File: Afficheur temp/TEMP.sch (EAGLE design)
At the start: 24 parts, among them IC1 MCP23008P, IC2 MCP23008P, X1 22-23-2041

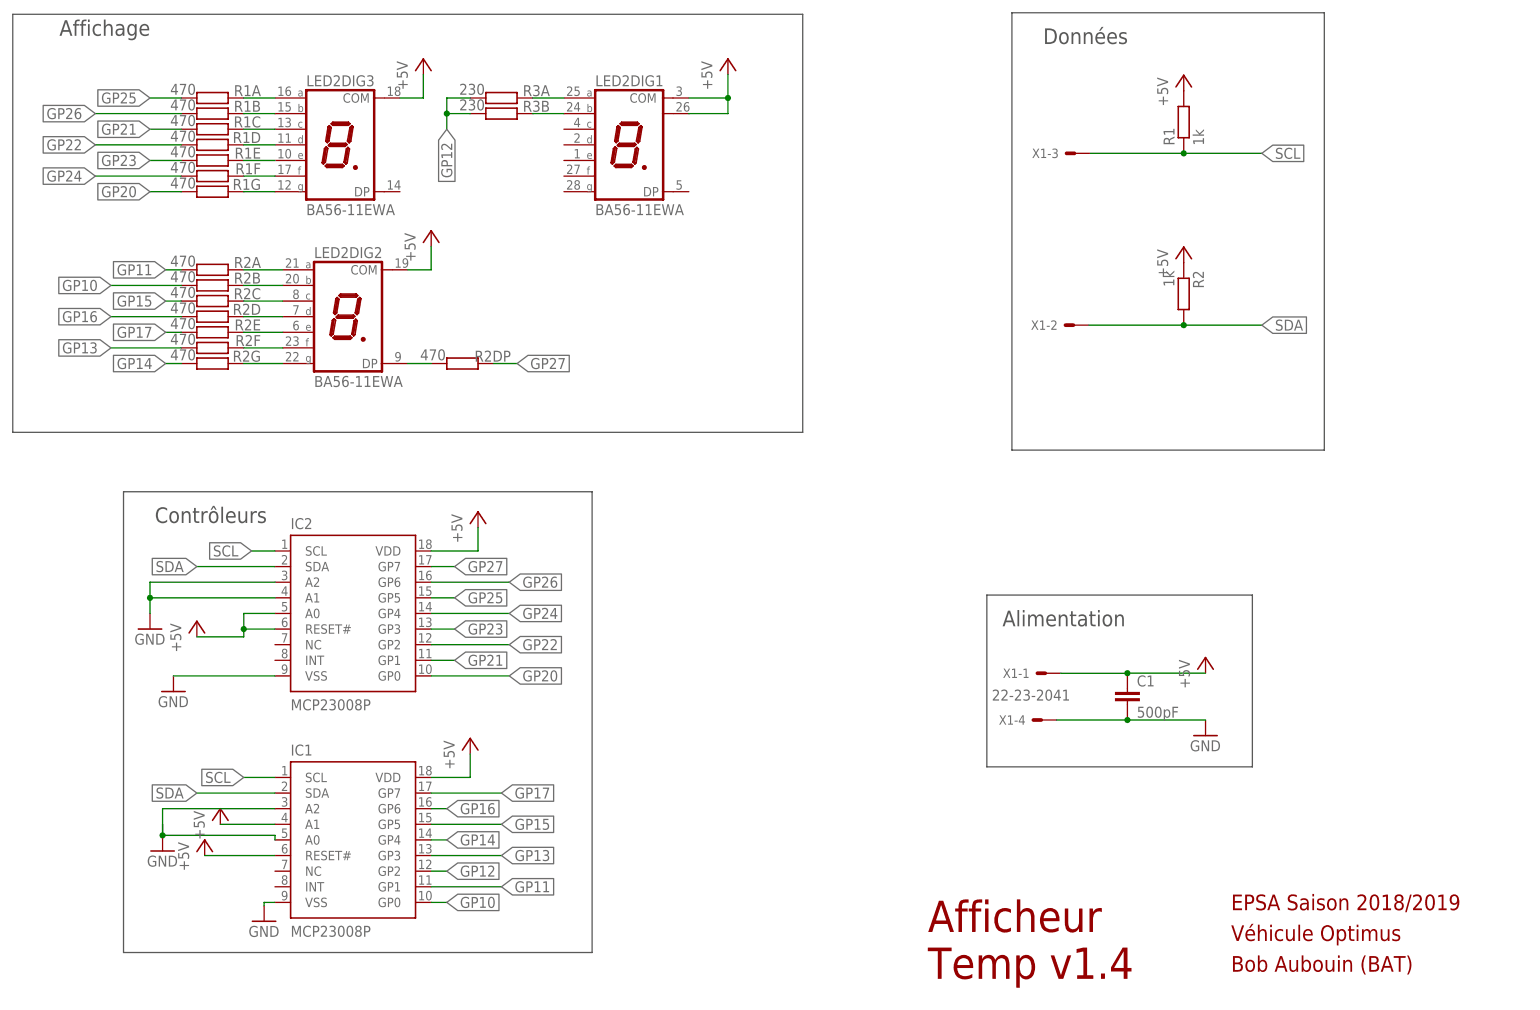
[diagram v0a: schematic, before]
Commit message: Supprsion des résistance de pull-up et MAJ des condos de lissage
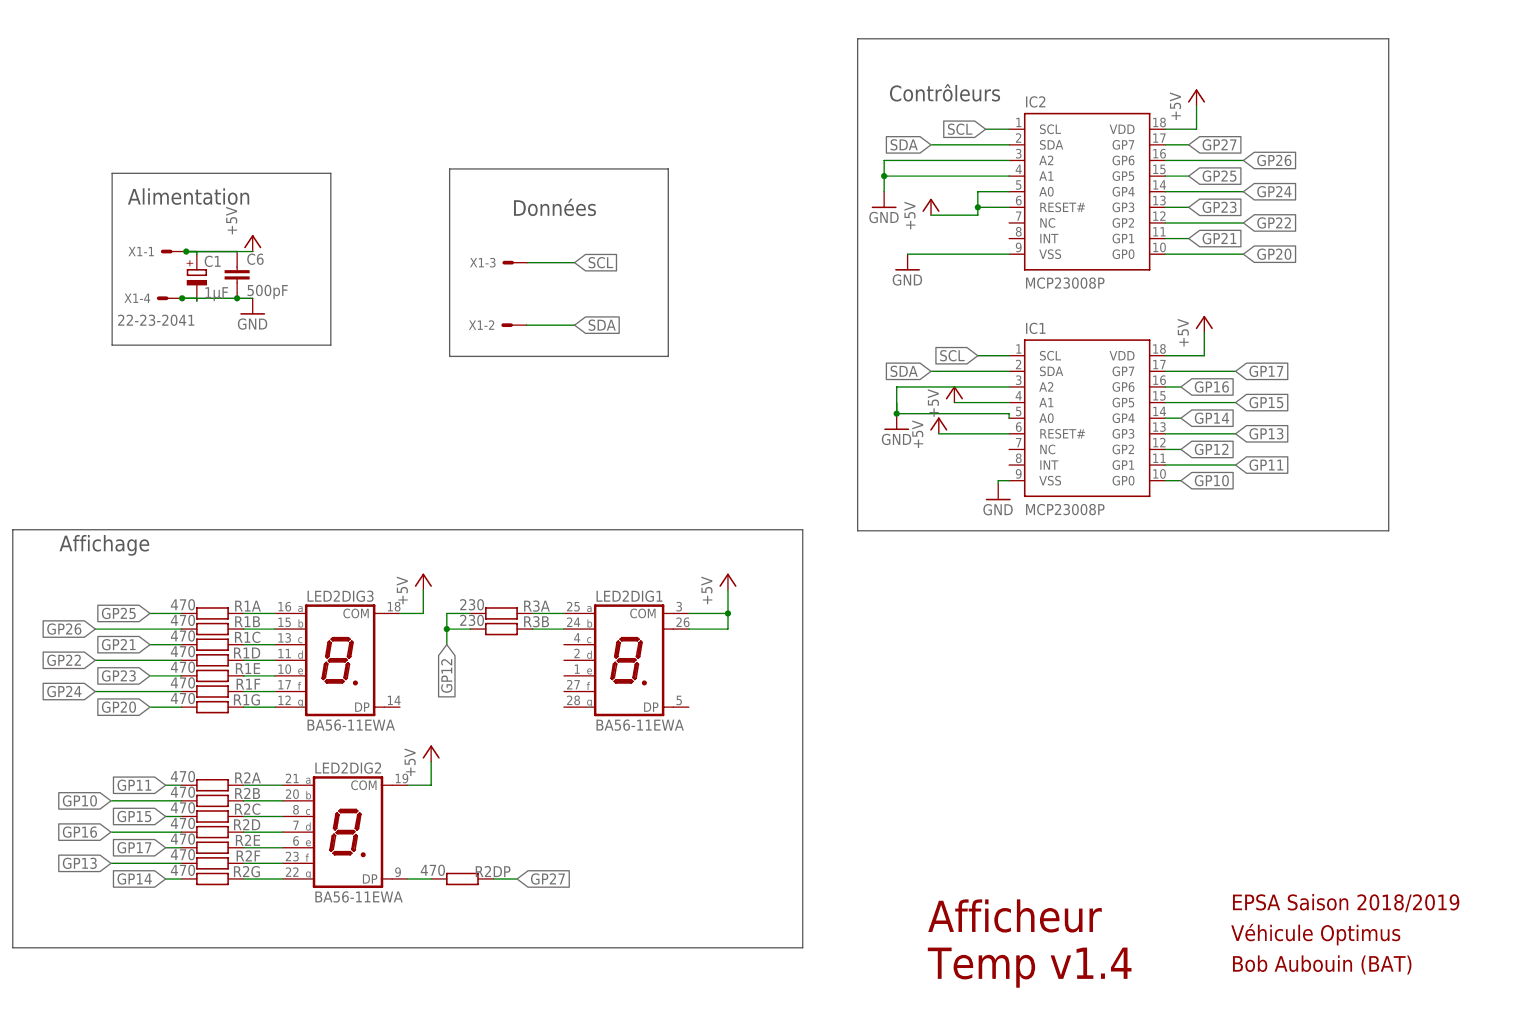
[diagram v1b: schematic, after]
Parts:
- removed R1, R2: 1k, rcl:R-EU_0204/7
- added C6: 500pF, rcl:C-EU025-025X050
- C1: value 500pF -> 1µF; device rcl:C-EU025-025X050 -> resistor:CPOL-EUB45181A
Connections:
- net +5V: now also C1.+, C6.1; no longer C1.1, R1.2, R2.1
- net GND: now also C1.-, C6.2; no longer C1.2
- net SCL: no longer R1.1
- net SDA: no longer R2.2
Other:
- moved on the sheet: IC1, IC2, LED2DIG1, LED2DIG2, LED2DIG3, R1A, R1B, R1C, R1D, R1E, R1F, R1G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

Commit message: Homogénéisation du schéma
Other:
- note added: "Afficheur Temp v1.2-dev"
- note removed: "Afficheur Temp v1.4"
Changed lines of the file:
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@@
 <sheet>
 <plain>
-<text x="167.14" y="9.16" size="5.08" layer="94">Afficheur
-Temp v1.4</text>
+<text x="169.68" y="9.16" size="3.81" layer="94">Afficheur Temp
+v1.2-dev</text>
 <text x="216.44" y="20.32" size="2.54" layer="94">EPSA Saison 2018/2019</text>
 <wire x1="89.36" y1="140.86" x2="89.36" y2="110.38" width="0.1524" layer="97"/>

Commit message: Mise en qualité
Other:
- note added: "Afficheur Temp v1.0"
- note removed: "Afficheur Temp v1.2-dev"
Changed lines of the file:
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@@
 <plain>
 <text x="169.68" y="9.16" size="3.81" layer="94">Afficheur Temp
-v1.2-dev</text>
+v1.0</text>
 <text x="216.44" y="20.32" size="2.54" layer="94">EPSA Saison 2018/2019</text>
 <wire x1="89.36" y1="140.86" x2="89.36" y2="110.38" width="0.1524" layer="97"/>

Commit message: Ajout des fichiers d'usinage et du readme
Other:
- note added: "EPSA Saison 2019"
- note added: "OPTIMUS v1.0"
- note removed: "EPSA Saison 2018/2019"
- note removed: "Véhicule Optimus"
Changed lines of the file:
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@@
 <text x="169.68" y="9.16" size="3.81" layer="94">Afficheur Temp
 v1.0</text>
-<text x="216.44" y="20.32" size="2.54" layer="94">EPSA Saison 2018/2019</text>
+<text x="216.44" y="20.32" size="2.54" layer="94">EPSA Saison 2019</text>
 <wire x1="89.36" y1="140.86" x2="89.36" y2="110.38" width="0.1524" layer="97"/>
 <wire x1="124.92" y1="110.38" x2="124.92" y2="140.86" width="0.1524" layer="97"/>
@@
 <wire x1="146.78" y1="82.19" x2="146.78" y2="14.21" width="0.1524" layer="97"/>
 <text x="25.9" y="78.69" size="2.54" layer="97">Affichage</text>
-<text x="216.44" y="15.32" size="2.54" layer="94">Véhicule Optimus</text>
+<text x="216.44" y="15.32" size="2.54" layer="94">OPTIMUS v1.0</text>
 <text x="216.44" y="10.32" size="2.54" layer="94">Bob Aubouin (BAT)</text>
 </plain>

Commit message: Passage à la version de dev suivante
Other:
- note added: "Afficheur Temp v1.1-dev"
- note removed: "Afficheur Temp v1.0"
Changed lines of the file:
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@@
 <plain>
 <text x="169.68" y="9.16" size="3.81" layer="94">Afficheur Temp
-v1.0</text>
+v1.1-dev</text>
 <text x="216.44" y="20.32" size="2.54" layer="94">EPSA Saison 2019</text>
 <wire x1="89.36" y1="140.86" x2="89.36" y2="110.38" width="0.1524" layer="97"/>
